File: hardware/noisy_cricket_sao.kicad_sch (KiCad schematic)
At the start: 19 parts, among them J1 Debug Pogo 6-Pin, J2 SAO 6-Pin, U1 AD8107, U2 CH32V003F4U6

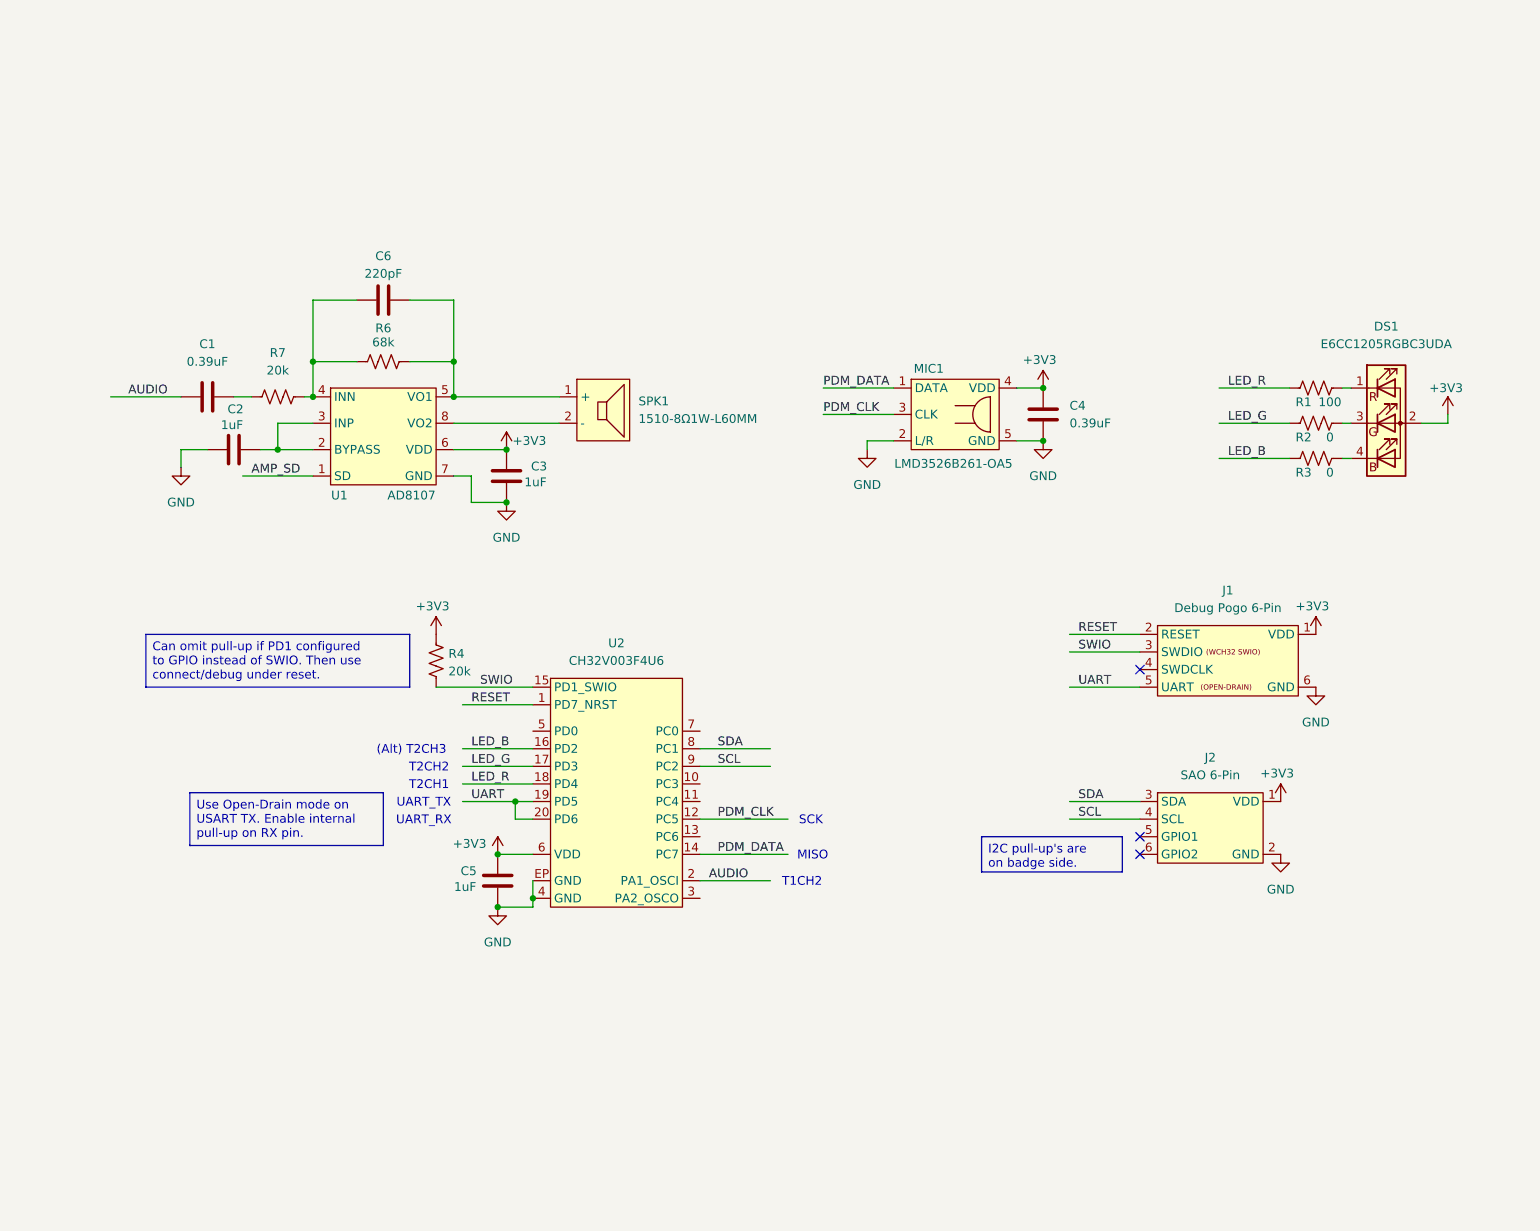
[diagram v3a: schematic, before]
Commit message: Add footprints and models, start part positioning.
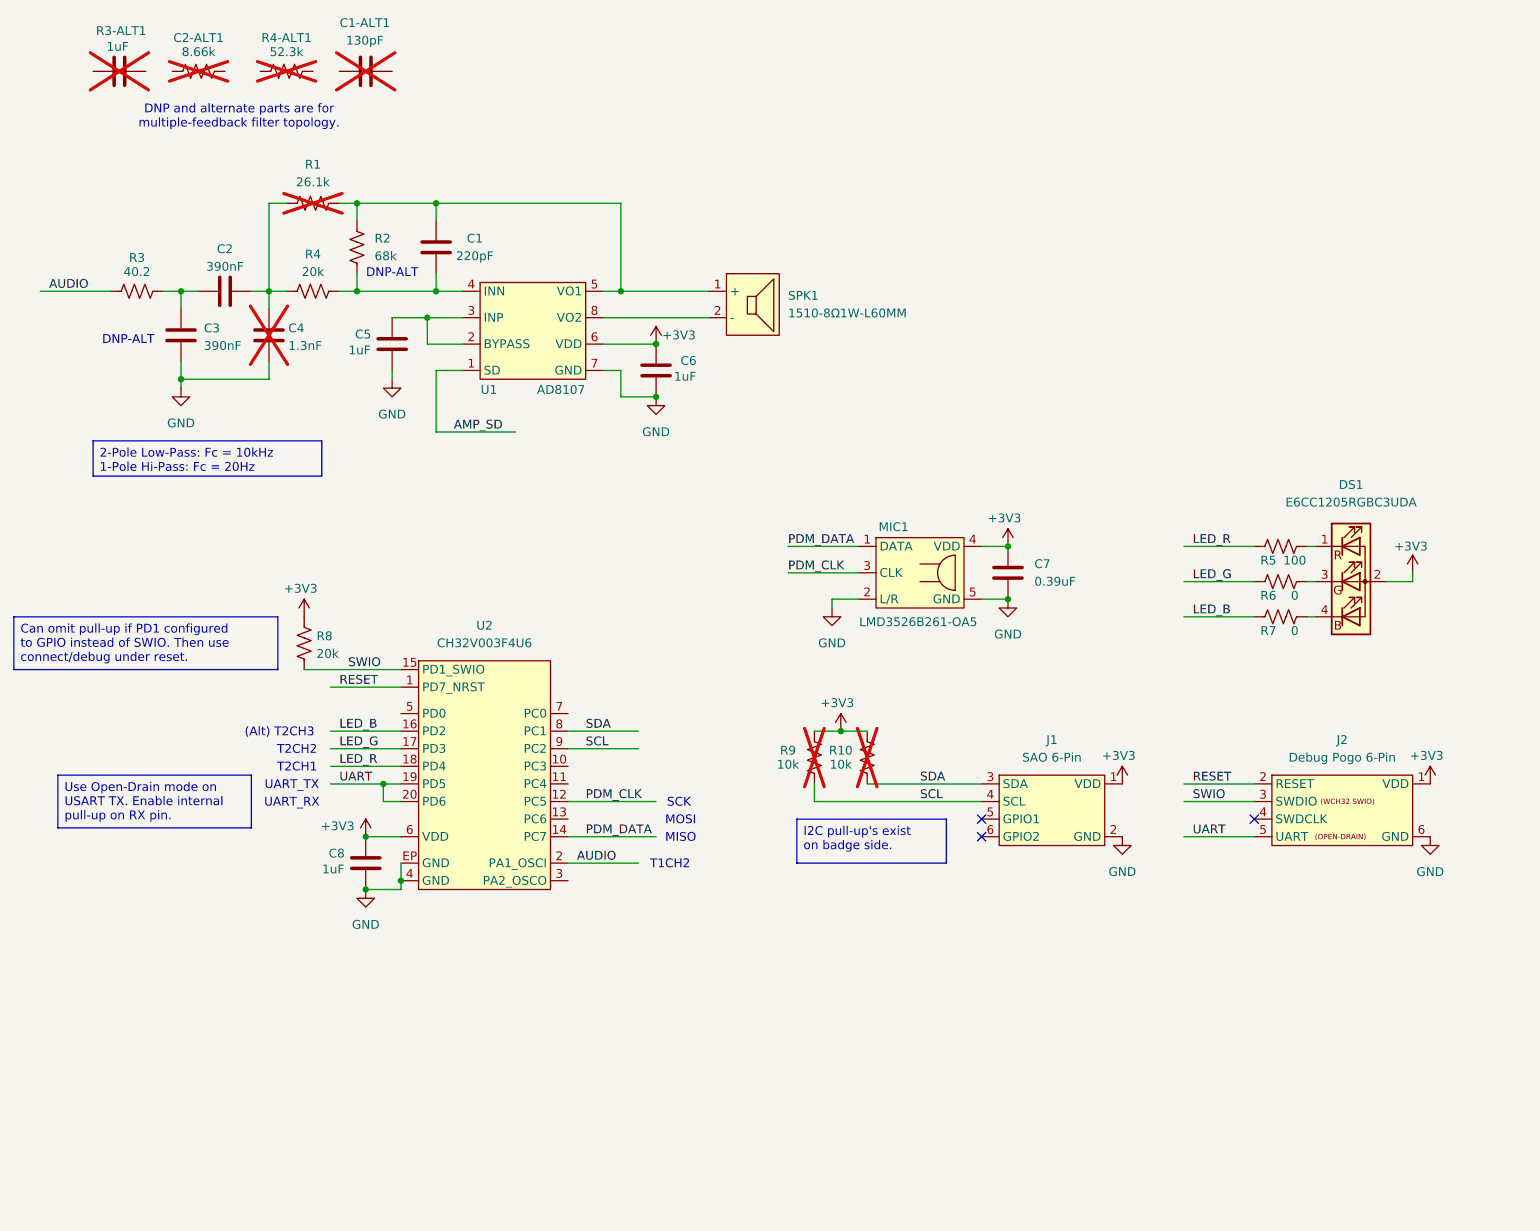
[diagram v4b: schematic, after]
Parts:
- removed R6: 68k, Resistor_SMD:R_0402_1005Metric, symbol Device:R_US
- added C1-ALT1: 130pF, Capacitor_SMD:C_0402_1005Metric, symbol Device:C
- added C2-ALT1: 8.66k, Resistor_SMD:R_0402_1005Metric, symbol Device:R_US
- added C3: 390nF, Capacitor_SMD:C_0402_1005Metric, symbol Device:C
- added C4: 1.3nF, Capacitor_SMD:C_0402_1005Metric, symbol Device:C
- added R1: 26.1k, Resistor_SMD:R_0402_1005Metric, symbol Device:R_US
- added R10, R9: 10k, Resistor_SMD:R_0402_1005Metric, symbol Device:R_US
- added R2: 68k, Resistor_SMD:R_0402_1005Metric, symbol Device:R_US
- added R3: 40.2, Resistor_SMD:R_0402_1005Metric, symbol Device:R_US
- added R3-ALT1: 1uF, Capacitor_SMD:C_0402_1005Metric, symbol Device:C
- added R4-ALT1: 52.3k, Resistor_SMD:R_0402_1005Metric, symbol Device:R_US
- C2: renamed from C1; value 0.39uF -> 390nF
- DS1: footprint (none) -> noisy_cricket_sao:E6CC1205RGBC3UDA
- J1: renamed from J2; footprint (none) -> Connector_PinHeader_2.54mm:PinHeader_2x03_P2.54mm_Vertical_SMD
- J2: renamed from J1; footprint (none) -> noisy_cricket_sao:Debug Pogo 6-Pin
- MIC1: footprint (none) -> noisy_cricket_sao:LMD3526B261-OA5
- SPK1: footprint (none) -> noisy_cricket_sao:1510-8Ω1W-L60MM
- U1: footprint (none) -> noisy_cricket_sao:AD8107
- U2: footprint (none) -> noisy_cricket_sao:CH32V003F4U6
- renumbered C6 to C1, C2 to C5, C3 to C6, C4 to C7, C5 to C8, R7 to R4, R1 to R5, R2 to R6, R3 to R7, R4 to R8
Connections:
- net +3V3: now also R10.2, R9.2
- net AUDIO: now also R3.1; no longer C2.1
- net GND: now also C3.2, C4.2
- net SCL: now also R9.1
- net SDA: now also R10.1
- net at R4.2, U1.4 (INN): now also C1.2, R2.1; no longer C1.1
- net at SPK1.1 (+), U1.5 (VO1): now also C1.1, R1.2, R2.2; no longer C1.2
- net at C2.2, R4.1: now also C4.1, R1.1
- new net: C2.1, C3.1, R3.2
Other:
- note added: "DNP and alternate parts are for multiple-feedback filter topology."
- note added: "DNP-ALT"
- note added: "MOSI"
- moved on the sheet: C1, C2, C5, C6, C7, C8, DS1, J1, J2, MIC1, R4, R5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

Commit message: Initial ugly routing of PCB
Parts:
- added MECH1: 1510-8Ω1W-L60MM_MECH, noisy_cricket_sao:1510-8Ω1W-L60MM_MECH, symbol noisy_cricket_sao:1510-8Ω1W-L60MM_MECH
- SPK1: footprint noisy_cricket_sao:1510-8Ω1W-L60MM -> noisy_cricket_sao:1510-8Ω1W-L60MM_SMT_PADS
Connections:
- net AMP_SD: now also U2.3 (PA2_OSCO)
- net GND: now also U1.9 (EP), U2.21 (GND); no longer U2.EP (GND)
- net LED_B: now also U2.18 (PD4); no longer U2.16 (PD2)
- net LED_R: now also U2.16 (PD2); no longer U2.18 (PD4)
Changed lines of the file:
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@@
 	(wire
 		(pts
+			(xy 102.87 138.43) (xy 113.03 138.43)
+		)
+		(stroke
+			(width 0)
+			(type default)
+		)
+	)
+	(wire
+		(pts
 			(xy 83.82 73.66) (xy 83.82 64.77)
 		)
@@
 		)
 	)
+	(label "AMP_SD"
+		(at 104.14 138.43 0)
+		(effects
+			(font
+				(size 1.27 1.27)
+			)
+			(justify left bottom)
+		)
+	)
 	(label "LED_B"
-		(at 69.85 116.84 0)
+		(at 69.85 121.92 0)
 		(effects
 			(font
@@
 		)
 	)
-	(label "AUDIO"
-		(at 27.94 53.34 0)
+	(label "LED_R"
+		(at 69.85 116.84 0)
 		(effects
 			(font
@@
 	)
 	(label "AUDIO"
-		(at 104.14 135.89 0)
+		(at 27.94 53.34 0)
 		(effects
 			(font
@@
 		)
 	)
-	(label "RESET"
-		(at 69.85 110.49 0)
+	(label "AUDIO"
+		(at 104.14 135.89 0)
 		(effects
 			(font
@@
 		)
 	)
-	(label "LED_R"
-		(at 69.85 121.92 0)
+	(label "RESET"
+		(at 69.85 110.49 0)
 		(effects
 			(font
@@
 		)
 		(instances
-			(project ""
+			(project "noisy_cricket_sao"
 				(path "/3f7eb731-322c-463d-a9ad-01b80ab04f9c"
 					(reference "R7")
@@
 		)
 		(instances
-			(project ""
+			(project "noisy_cricket_sao"
 				(path "/3f7eb731-322c-463d-a9ad-01b80ab04f9c"
 					(reference "#PWR02")
@@
 		)
 		(instances
-			(project ""
+			(project "noisy_cricket_sao"
 				(path "/3f7eb731-322c-463d-a9ad-01b80ab04f9c"
 					(reference "#PWR01")
@@
 		)
 		(instances
-			(project ""
+			(project "noisy_cricket_sao"
 				(path "/3f7eb731-322c-463d-a9ad-01b80ab04f9c"
 					(reference "MIC1")
@@
 		(pin "4"
 		)
+		(pin "9"
+		)
 		(instances
-			(project ""
+			(project "noisy_cricket_sao"
 				(path "/3f7eb731-322c-463d-a9ad-01b80ab04f9c"
 					(reference "U1")
@@
 		)
 		(instances
-			(project ""
+			(project "noisy_cricket_sao"
 				(path "/3f7eb731-322c-463d-a9ad-01b80ab04f9c"
 					(reference "R6")
@@
 		)
 		(instances
-			(project ""
+			(project "noisy_cricket_sao"
 				(path "/3f7eb731-322c-463d-a9ad-01b80ab04f9c"
 					(reference "DS1")
@@
 	)
 	(symbol
-		(lib_id "noisy_cricket_sao:Debug Pogo 6-Pin")
-		(at 214.63 128.27 0)
-		(unit 1)
-		(exclude_from_sim no)
-		(in_bom yes)
-		(on_board yes)
-		(dnp no)
-		(fields_autoplaced yes)
-		(property "Reference" "J2"
-			(at 214.63 118.11 0)
-			(effects
-				(font
-					(size 1.27 1.27)
-				)
-			)
-		)
-		(property "Value" "Debug Pogo 6-Pin"
-			(at 214.63 120.65 0)
-			(effects
-				(font
-					(size 1.27 1.27)
-				)
-			)
-		)
-		(property "Footprint" "noisy_cricket_sao:Debug Pogo 6-Pin"
-			(at 214.63 128.27 0)
-			(effects
-				(font
-					(size 1.27 1.27)
-				)
-				(hide yes)
-			)
-		)
-		(property "Datasheet" ""
-			(at 214.63 128.27 0)
-			(effects
-				(font
-					(size 1.27 1.27)
-				)
-				(hide yes)
-			)
-		)
-		(property "Description" ""
-			(at 214.63 128.27 0)
-			(effects
-				(font
-					(size 1.27 1.27)
-				)
-				(hide yes)
-			)
-		)
-		(pin "6"
-		)
-		(pin "5"
-		)
-		(pin "4"
-		)
-		(pin "3"
-		)
-		(pin "2"
-		)
-		(pin "1"
-		)
-		(instances
-			(project ""
-				(path "/3f7eb731-322c-463d-a9ad-01b80ab04f9c"
-					(reference "J2")
-					(unit 1)
-				)
-			)
-		)
-	)
-	(symbol
 		(lib_id "power:GND")
 		(at 115.57 68.58 0)
@@
 		)
 		(instances
-			(project ""
+			(project "noisy_cricket_sao"
 				(path "/3f7eb731-322c-463d-a9ad-01b80ab04f9c"
 					(reference "R5")
@@
 		(pin "10"
 		)
-		(pin "EP"
+		(pin "21"
 		)
 		(pin "9"
@@
 		)
 		(instances
-			(project ""
+			(project "noisy_cricket_sao"
 				(path "/3f7eb731-322c-463d-a9ad-01b80ab04f9c"
 					(reference "U2")
@@
 			)
 		)
-		(property "Footprint" "noisy_cricket_sao:1510-8Ω1W-L60MM"
+		(property "Footprint" "noisy_cricket_sao:1510-8Ω1W-L60MM_SMT_PADS"
 			(at 129.54 54.61 0)
 			(effects
@@
 		)
 		(instances
-			(project ""
+			(project "noisy_cricket_sao"
 				(path "/3f7eb731-322c-463d-a9ad-01b80ab04f9c"
 					(reference "SPK1")
@@
 	)
 	(symbol
+		(lib_id "noisy_cricket_sao:1510-8Ω1W-L60MM_MECH")
+		(at 129.54 33.02 0)
+		(unit 1)
+		(exclude_from_sim no)
+		(in_bom no)
+		(on_board yes)
+		(dnp no)
+		(property "Reference" "MECH1"
+			(at 127.508 28.194 0)
+			(effects
+				(font
+					(size 1.27 1.27)
+				)
+				(hide yes)
+			)
+		)
+		(property "Value" "1510-8Ω1W-L60MM_MECH"
+			(at 118.872 41.402 0)
+			(effects
+				(font
+					(size 1.27 1.27)
+				)
+				(justify left)
+			)
+		)
+		(property "Footprint" "noisy_cricket_sao:1510-8Ω1W-L60MM_MECH"
+			(at 129.54 33.02 0)
+			(effects
+				(font
+					(size 1.27 1.27)
+				)
+				(hide yes)
+			)
+		)
+		(property "Datasheet" "https://www.lcsc.com/datasheet/C49246975.pdf"
+			(at 128.27 24.13 0)
+			(effects
+				(font
+					(size 1.27 1.27)
+				)
+				(hide yes)
+			)
+		)
+		(property "Description" "PCB Holes and 3D Model for: 15x10mm 8Ω Electromagnetic 900Hz 88dB 1W Speakers RoHS"
+			(at 128.27 24.13 0)
+			(effects
+				(font
+					(size 1.27 1.27)
+				)
+				(hide yes)
+			)
+		)
+		(instances
+			(project "noisy_cricket_sao"
+				(path "/3f7eb731-322c-463d-a9ad-01b80ab04f9c"
+					(reference "MECH1")
+					(unit 1)
+				)
+			)
+		)
+	)
+	(symbol
 		(lib_id "Device:R_US")
 		(at 66.04 40.64 90)
@@
 		)
 		(instances
-			(project ""
+			(project "noisy_cricket_sao"
 				(path "/3f7eb731-322c-463d-a9ad-01b80ab04f9c"
 					(reference "R8")
@@
 		)
 		(instances
-			(project ""
+			(project "noisy_cricket_sao"
 				(path "/3f7eb731-322c-463d-a9ad-01b80ab04f9c"
 					(reference "J1")
@@
 	)
 	(symbol
+		(lib_id "noisy_cricket_sao:Debug Pogo 6-Pin")
+		(at 214.63 128.27 0)
+		(unit 1)
+		(exclude_from_sim no)
+		(in_bom yes)
+		(on_board yes)
+		(dnp no)
+		(fields_autoplaced yes)
+		(property "Reference" "J2"
+			(at 214.63 118.11 0)
+			(effects
+				(font
+					(size 1.27 1.27)
+				)
+			)
+		)
+		(property "Value" "Debug Pogo 6-Pin"
+			(at 214.63 120.65 0)
+			(effects
+				(font
+					(size 1.27 1.27)
+				)
+			)
+		)
+		(property "Footprint" "noisy_cricket_sao:Debug Pogo 6-Pin"
+			(at 214.63 128.27 0)
+			(effects
+				(font
+					(size 1.27 1.27)
+				)
+				(hide yes)
+			)
+		)
+		(property "Datasheet" ""
+			(at 214.63 128.27 0)
+			(effects
+				(font
+					(size 1.27 1.27)
+				)
+				(hide yes)
+			)
+		)
+		(property "Description" ""
+			(at 214.63 128.27 0)
+			(effects
+				(font
+					(size 1.27 1.27)
+				)
+				(hide yes)
+			)
+		)
+		(pin "5"
+		)
+		(pin "3"
+		)
+		(pin "1"
+		)
+		(pin "2"
+		)
+		(pin "6"
+		)
+		(pin "4"
+		)
+		(instances
+			(project "noisy_cricket_sao"
+				(path "/3f7eb731-322c-463d-a9ad-01b80ab04f9c"
+					(reference "J2")
+					(unit 1)
+				)
+			)
+		)
+	)
+	(symbol
 		(lib_id "power:+3V3")
 		(at 73.66 132.08 0)
@@
 		)
 		(instances
-			(project ""
+			(project "noisy_cricket_sao"
 				(path "/3f7eb731-322c-463d-a9ad-01b80ab04f9c"
 					(reference "C2")

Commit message: 2nd ugly route complete
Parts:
- removed J2: Debug Pogo 6-Pin, noisy_cricket_sao:Debug Pogo 6-Pin, symbol noisy_cricket_sao:Debug Pogo 6-Pin
- removed R10, R9: 10k, Resistor_SMD:R_0402_1005Metric, symbol Device:R_US
- added FID1, FID2: Fiducial, Fiducial:Fiducial_0.5mm_Mask1.5mm, symbol Mechanical:Fiducial
- added TP1: TestPoint, TestPoint:TestPoint_Pad_D1.0mm, symbol Connector:TestPoint
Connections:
- net RESET: now also TP1.1
- net SWIO: now also J1.6 (GPIO2)
- net UART: now also J1.5 (GPIO1), U2.7 (PC0); no longer U2.19 (PD5), U2.20 (PD6)
- no-connect marks 3 -> 0
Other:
- note added: "UART_TX (Alt)"
- note removed: "UART_RX"
- note removed: "UART_TX"
